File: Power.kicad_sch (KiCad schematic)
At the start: 78 parts, among them J3 DBT50G-9.5-2P, J38 2.54-1*4, J4 DBT50G-9.5-2P, J5 DBT50G-9.5-2P, J6 DBT50G-9.5-2P, U12 INA226, U13 INA226, U14 INA226, U15 INA226, U5 TPS63070RNMR

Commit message: Added footprints for resistors
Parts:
- C133, C134, C135, C136, C137, C138, C139, C140: Manufacturer (none) -> Murata; manufacturer Murata -> (none)
- C23, C24: Capacitance 22uF -> (none); capacitance (none) -> 22uF
- C25, C26, C29, C31, C32: Capacitance 10uF -> (none); capacitance (none) -> 10uF
- C27, C28, C30: Capacitance 100nF -> (none); capacitance (none) -> 100nF
- C33: Capacitance 47uF -> (none); capacitance (none) -> 47uF
- R14: footprint PixelBlit:R0402 -> PixelBlit:R_0402
- R22, R23, R55, R56, R57, R58, R59, R60, R61, R62, R63, R64: footprint (none) -> PixelBlit:R_0402
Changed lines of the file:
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@@
 			)
 		)
-		(property "Footprint" ""
+		(property "Footprint" "PixelBlit:R_0402"
 			(at 117.602 232.41 90)
 			(hide yes)
@@
 			)
 		)
-		(property "Capacitance" "10uF"
+		(property "capacitance" "10uF"
 			(at 137.16 71.12 0)
 			(hide yes)
@@
 			)
 		)
-		(property "Capacitance" "100nF"
+		(property "capacitance" "100nF"
 			(at 59.69 90.17 0)
 			(hide yes)
@@
 			)
 		)
-		(property "Capacitance" "10uF"
+		(property "capacitance" "10uF"
 			(at 97.79 143.51 0)
 			(hide yes)
@@
 			)
 		)
-		(property "Footprint" ""
+		(property "Footprint" "PixelBlit:R_0402"
 			(at 320.04 230.378 90)
 			(hide yes)
@@
 			)
 		)
-		(property "manufacturer" "Murata"
+		(property "Manufacturer" "Murata"
 			(at 382.27 214.63 0)
 			(hide yes)
@@
 			)
 		)
-		(property "manufacturer" "Murata"
+		(property "Manufacturer" "Murata"
 			(at 326.39 232.41 0)
 			(hide yes)
@@
 			)
 		)
-		(property "Footprint" ""
+		(property "Footprint" "PixelBlit:R_0402"
 			(at 227.33 230.378 90)
 			(hide yes)
@@
 			)
 		)
-		(property "manufacturer" "Murata"
+		(property "Manufacturer" "Murata"
 			(at 191.77 214.63 0)
 			(hide yes)
@@
 			)
 		)
-		(property "Footprint" ""
+		(property "Footprint" "PixelBlit:R_0402"
 			(at 320.04 237.998 90)
 			(hide yes)
@@
 			)
 		)
-		(property "Capacitance" "100nF"
+		(property "capacitance" "100nF"
 			(at 39.37 142.24 0)
 			(hide yes)
@@
 			)
 		)
-		(property "manufacturer" "Murata"
+		(property "Manufacturer" "Murata"
 			(at 289.56 214.63 0)
 			(hide yes)
@@
 			)
 		)
-		(property "Capacitance" "100nF"
+		(property "capacitance" "100nF"
 			(at 109.22 143.51 0)
 			(hide yes)
@@
 			)
 		)
-		(property "Capacitance" "47uF"
+		(property "capacitance" "47uF"
 			(at 146.05 71.12 0)
 			(hide yes)
@@
 			)
 		)
-		(property "Capacitance" "22uF"
+		(property "capacitance" "22uF"
 			(at 36.83 77.47 0)
 			(hide yes)
@@
 			)
 		)
-		(property "Footprint" ""
+		(property "Footprint" "PixelBlit:R_0402"
 			(at 308.102 232.41 90)
 			(hide yes)
@@
 			)
 		)
-		(property "Footprint" ""
+		(property "Footprint" "PixelBlit:R_0402"
 			(at 33.02 237.998 90)
 			(hide yes)
@@
 			)
 		)
-		(property "manufacturer" "Murata"
+		(property "Manufacturer" "Murata"
 			(at 95.25 214.63 0)
 			(hide yes)
@@
 			)
 		)
-		(property "Footprint" ""
+		(property "Footprint" "PixelBlit:R_0402"
 			(at 21.082 232.41 90)
 			(hide yes)
@@
 			)
 		)
-		(property "Capacitance" "10uF"
+		(property "capacitance" "10uF"
 			(at 128.27 71.12 0)
 			(hide yes)
@@
 			)
 		)
-		(property "Footprint" ""
+		(property "Footprint" "PixelBlit:R_0402"
 			(at 33.02 230.378 90)
 			(hide yes)
@@
 			)
 		)
-		(property "Footprint" "PixelBlit:R0402"
+		(property "Footprint" "PixelBlit:R_0402"
 			(at 114.3 63.5 0)
 			(hide yes)
@@
 			)
 		)
-		(property "Footprint" ""
+		(property "Footprint" "PixelBlit:R_0402"
 			(at 129.54 237.998 90)
 			(hide yes)
@@
 			)
 		)
-		(property "manufacturer" "Murata"
+		(property "Manufacturer" "Murata"
 			(at 39.37 232.41 0)
 			(hide yes)
@@
 			)
 		)
-		(property "Capacitance" "22uF"
+		(property "capacitance" "22uF"
 			(at 30.48 77.47 0)
 			(hide yes)
@@
 			)
 		)
-		(property "Capacitance" "10uF"
+		(property "capacitance" "10uF"
 			(at 30.48 142.24 0)
 			(hide yes)
@@
 			)
 		)
-		(property "manufacturer" "Murata"
+		(property "Manufacturer" "Murata"
 			(at 135.89 232.41 0)
 			(hide yes)
@@
 			)
 		)
-		(property "Capacitance" "10uF"
+		(property "capacitance" "10uF"
 			(at 46.99 77.47 0)
 			(hide yes)
@@
 			)
 		)
-		(property "Footprint" ""
+		(property "Footprint" "PixelBlit:R_0402"
 			(at 227.33 237.998 90)
 			(hide yes)
@@
 			)
 		)
-		(property "Footprint" ""
+		(property "Footprint" "PixelBlit:R_0402"
 			(at 215.392 232.41 90)
 			(hide yes)
@@
 			)
 		)
-		(property "manufacturer" "Murata"
+		(property "Manufacturer" "Murata"
 			(at 233.68 232.41 0)
 			(hide yes)
@@
 			)
 		)
-		(property "Footprint" ""
+		(property "Footprint" "PixelBlit:R_0402"
 			(at 129.54 230.378 90)
 			(hide yes)

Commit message: Updated 2m ohm resistors
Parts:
- R22, R56, R59, R62: footprint PixelBlit:R_0402 -> Resistor_SMD:R_Shunt_Vishay_WSK2512_6332Metric_T1.19mm
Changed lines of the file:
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@@
 			)
 		)
-		(property "Footprint" "PixelBlit:R_0402"
+		(property "Footprint" "Resistor_SMD:R_Shunt_Vishay_WSK2512_6332Metric_T1.19mm"
 			(at 117.602 232.41 90)
 			(hide yes)
@@
 			)
 		)
-		(property "Footprint" "PixelBlit:R_0402"
+		(property "Footprint" "Resistor_SMD:R_Shunt_Vishay_WSK2512_6332Metric_T1.19mm"
 			(at 308.102 232.41 90)
 			(hide yes)
@@
 			)
 		)
-		(property "Footprint" "PixelBlit:R_0402"
+		(property "Footprint" "Resistor_SMD:R_Shunt_Vishay_WSK2512_6332Metric_T1.19mm"
 			(at 21.082 232.41 90)
 			(hide yes)
@@
 			)
 		)
-		(property "Footprint" "PixelBlit:R_0402"
+		(property "Footprint" "Resistor_SMD:R_Shunt_Vishay_WSK2512_6332Metric_T1.19mm"
 			(at 215.392 232.41 90)
 			(hide yes)

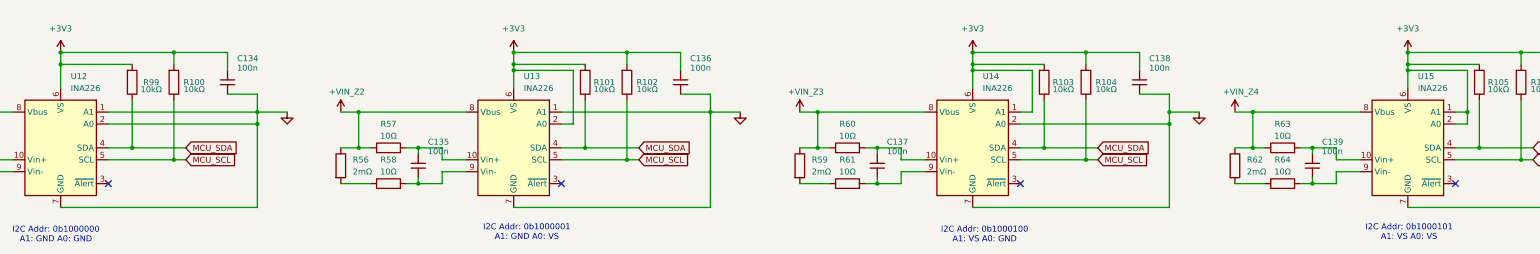
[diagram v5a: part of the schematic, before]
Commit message: Fix SDA/SCL swap and floating I2C pins in the schematic
universal-strip-controller.kicad_sch:
- Swapped the MCU_SDA/MCU_SCL global labels at the RP2350B's GPIO38/GPIO39
  pins, so the net names now match the RP2350's silicon-fixed I2C1 SDA/SCL
  roles (GPIO38=SDA, GPIO39=SCL) instead of the reverse. Only the two
  label instances at the MCU end needed changing -- KiCad global labels
  connect by name project-wide, so every pull-up resistor, the DS3231, and
  all four INA226s automatically picked up the corrected net.
- Wired the DS3231's SDA (pin 15) and SCL (pin 16) pins to the MCU_SDA/
  MCU_SCL nets -- both were previously unconnected (SDA had no wire at
  all; SCL had a stray no_connect flag, now removed).

Power.kicad_sch:
- Added the one missing stub wire per channel connecting each of the four
  INA226s' SCL pin to the already-otherwise-complete MCU_SCL pull-up/label
  network (only SDA had been wired through).

Verified by re-parsing both files and re-tracing nets (including modeling
KiCad's name-based global label connectivity, not just physical wire
paths): GPIO38 and the DS3231/all four INA226 SDA pins are one net;
GPIO39 and their SCL pins are a separate net, as intended.

Caught and fixed a bug of my own along the way: the INA226 SCL fix's
first attempt routed a new wire straight through the neighboring SDA
pin's coordinate (same column, passing through on the way to the existing
pull-up junction), which would have shorted SDA to SCL on all four
channels. Rerouted with a jog to a clear column instead.

Not fixed, left as an open item (documented in firmware/README.md): the
four INA226s' A0/A1 address pins are still all floating, so all four
currently default to the same I2C address. Restoring the SDA/SCL
connections was "obviously intended, just missing a wire" -- assigning
per-channel addresses is a design decision, so it's left for a deliberate
follow-up rather than guessed at here.

Also updated firmware/README.md and the example comments, which
docu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
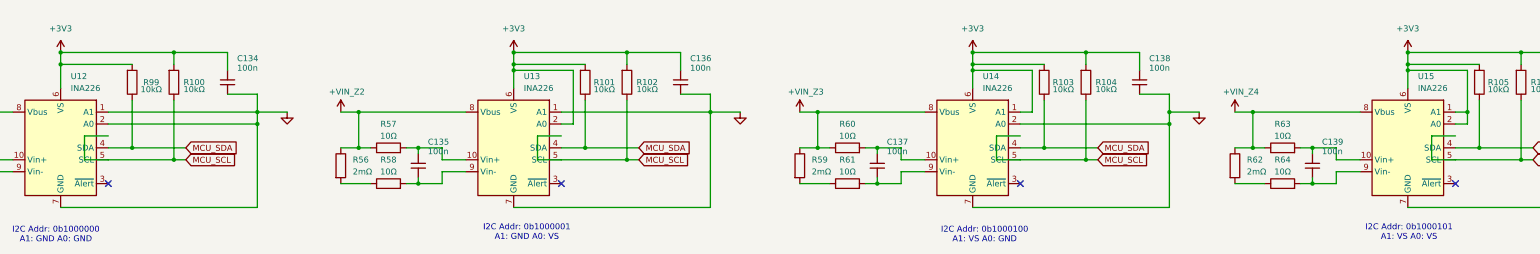
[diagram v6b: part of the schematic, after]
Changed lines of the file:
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@@
+	(wire
+		(pts
+			(xy 356.87 226.06) (xy 351.79 226.06) (xy 351.79 231.14) (xy 356.87 231.14)
+		)
+		(stroke
+			(width 0)
+			(type default)
+		)
+	)
 	(wire
 		(pts
@@
 	(wire
 		(pts
+			(xy 166.37 226.06) (xy 161.29 226.06) (xy 161.29 231.14) (xy 166.37 231.14)
+		)
+		(stroke
+			(width 0)
+			(type default)
+		)
+	)
+	(wire
+		(pts
 			(xy 95.25 217.17) (xy 101.6 217.17)
 		)
@@
 	(wire
 		(pts
+			(xy 264.16 226.06) (xy 259.08 226.06) (xy 259.08 231.14) (xy 264.16 231.14)
+		)
+		(stroke
+			(width 0)
+			(type default)
+		)
+	)
+	(wire
+		(pts
 			(xy 289.56 217.17) (xy 295.91 217.17)
 		)
@@
 		)
 		(stroke
+			(width 0)
+			(type default)
+		)
+	)
+	(wire
+		(pts
+			(xy 69.85 226.06) (xy 64.77 226.06) (xy 64.77 231.14) (xy 69.85 231.14)
+		)
+		(stroke

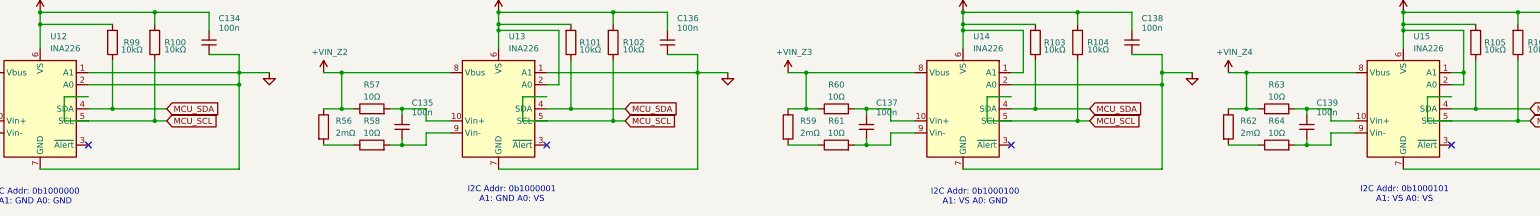
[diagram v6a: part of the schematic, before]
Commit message: Wire INA226 A0/A1 to match the schematic's own documented address scheme
Power.kicad_sch already had text annotations next to each of the four
INA226s spelling out the intended per-channel address (0x40/0x41/0x44/
0x45, via A1 and A0 each tied to GND or VS) -- I'd missed these entirely
in the previous pass since I was only looking at electrical objects
(wires/labels/pins), not schematic text notes.

Checking the actual A0/A1 wiring against that documented plan turned up a
real bug: channels 3 and 4 (U14, U15) need A1 tied to VS, but both had a
no_connect flag on A1 instead (which reads as GND), so as wired they'd
have collided with channels 1 and 2. This took three rounds of back and
forth to pin down -- thanks for pushing back and asking for the exact
coordinate check, since it settled definitively (matching, byte-for-byte,
on both ends) that the file really did have it wrong, not that I was
misreading it.

Fixed all four channels to match the documented scheme:
- U12 (0x40): A1=GND, A0=GND -- both already-correct no_connect flags
  (A1 unchanged) plus one added for A0.
- U13 (0x41): A1=GND (unchanged), A0 wired to VS.
- U14 (0x44): A1's incorrect no_connect removed and wired to VS instead;
  A0 given a no_connect flag for GND.
- U15 (0x45): A1's incorrect no_connect removed; A0 and A1 both wired to
  VS (one wire run, since they're the same net here).

Routed carefully around the lesson from the SDA/SCL fix: A0 and A1 sit in
the same column 2.54mm apart, so a naive straight wire to VS from one
would cross and short the other on channels where they need to differ
(U13, U14) -- jogged sideways there. Where both pins genuinely need the
same net (U15), ran it straight through since that's a real connection,
not a short.

Verified by re-tracing nets: all four chips now resolve to their distinct
documented addresses, and the earlier SDA/SCL fix is unaffected.
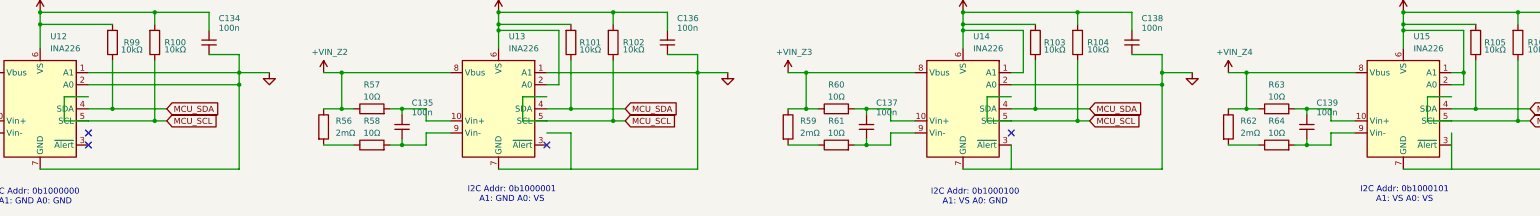
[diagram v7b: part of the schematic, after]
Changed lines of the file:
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@@
 	)
 	(no_connect
-		(at 356.87 236.22)
-	)
-	(no_connect
-		(at 264.16 236.22)
+		(at 264.16 233.68)
 	)
 	(no_connect
@@
 	)
 	(no_connect
+		(at 69.85 233.68)
+	)
+	(no_connect
 		(at 90.17 139.7)
 	)
@@
 	(wire
 		(pts
+			(xy 264.16 236.22) (xy 264.16 241.3)
+		)
+		(stroke
+			(width 0)
+			(type default)
+		)
+	)
+	(wire
+		(pts
 			(xy 359.41 220.98) (xy 359.41 212.09)
 		)
@@
 	(wire
 		(pts
+			(xy 356.87 233.68) (xy 356.87 241.3)
+		)
+		(stroke
+			(width 0)
+			(type default)
+		)
+	)
+	(wire
+		(pts
 			(xy 162.56 50.8) (xy 165.1 50.8)
 		)
@@
 		)
 		(stroke
+			(width 0)
+			(type default)
+		)
+	)
+	(wire
+		(pts
+			(xy 166.37 233.68) (xy 171.45 233.68) (xy 171.45 241.3)
+		)
+		(stroke
